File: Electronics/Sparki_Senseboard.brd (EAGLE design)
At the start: 88.7 x 17.1 mm, 21 parts

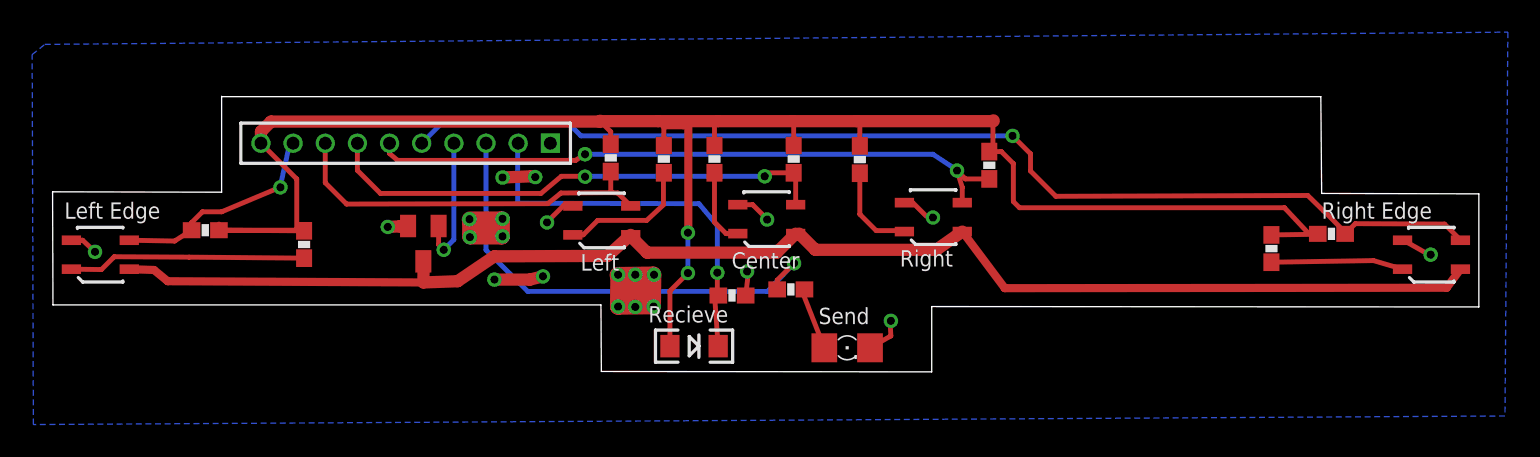
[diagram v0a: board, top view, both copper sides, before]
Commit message: Updated connectors, sensor multiplexing
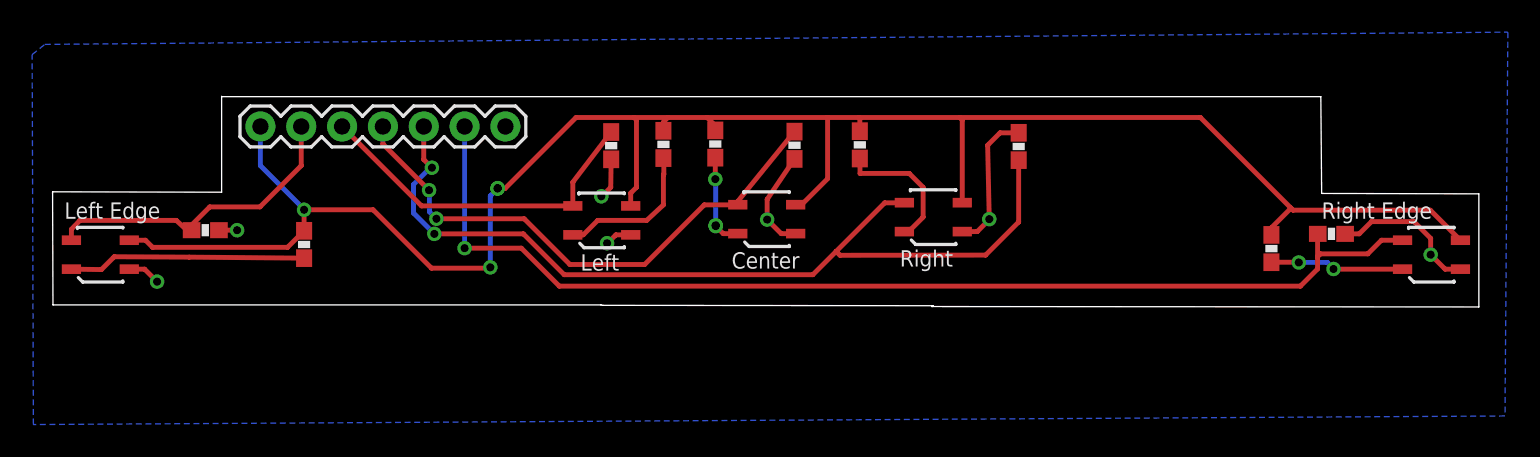
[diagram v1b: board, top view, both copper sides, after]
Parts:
- removed D4: IR_GRAB_LED, arcbotics:FKIT-LED-1206
- removed Q9: (no value), adafruit:SOT23
- removed R25: 100, SparkFun-Passives:0603-RES
- removed R26: 10k, SparkFun-Passives:0603-RES
- removed U$17: IR_GRAB_SENSE, arcbotics:LED-1206
- JP1: value M102MM -> (none); device arcbotics:1X10-2MM -> SparkFun-Connectors:1X07
- moved JP1 2.98 mm to (-16.3, 5.79)
- moved R16 2.17 mm to (15.6, 4.55), turned to 90 degrees
- moved R14 0.94 mm to (-3.23, 4.70)
- moved R15 0.91 mm to (-6.45, 4.67)
- moved R13 0.91 mm to (5.77, 4.65)
- moved R17 0.87 mm to (1.70, 4.62)
- moved R18 0.76 mm to (-9.70, 4.60)
- turned R21 to 0 degrees
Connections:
- removed net IR_GRAB_LED: JP1.3, R25.1
- removed net IR_GRAB_SENSE: JP1.2, R26.1, U$17.C
- removed net IR_SWITCH: JP1.4, Q9.1
- removed net N$25: Q9.3, U$10.2, U$4.2, U$5.2, U$6.2, U$9.2
- removed net N$33: D4.A, R25.2
- net GND: now also R16.2, R17.2, R18.2, R20.2, R21.2, U$10.2, U$4.2, U$5.2, U$6.2, U$9.2; no longer D4.C, Q9.2, R26.2, U$10.4, U$4.4, U$5.4, U$6.4, U$9.4
- net PB4: now also JP1.5, R18.1, U$6.4; no longer JP1.8, R18.2, U$6.3
- net PD4: now also JP1.3, R16.1, U$4.4; no longer JP1.6, R16.2, U$4.3
- net PD6: now also JP1.4, R17.1, U$5.4; no longer JP1.7, R17.2, U$5.3
- net PF5: now also JP1.6, R21.1, U$9.4; no longer JP1.9, R21.2, U$9.3
- net PF6: now also JP1.2, R20.1, U$10.4; no longer JP1.5, R20.2, U$10.3
- net VCC: now also JP1.7, U$10.3, U$4.3, U$5.3, U$6.3, U$9.3; no longer JP1.10, R16.1, R17.1, R18.1, R20.1, R21.1, U$17.A
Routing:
- net N$25: track 89.5 -> 0.00 mm
- net IR_GRAB_LED: track 29.6 -> 0.00 mm, vias 1 -> 0
- net IR_GRAB_SENSE: track 24.4 -> 0.00 mm, vias 1 -> 0
- net PD4: track 40.8 -> 56.3 mm
- net IR_SWITCH: track 8.50 -> 0.00 mm, vias 1 -> 0
- net GND: track 40.5 -> 32.0 mm, vias 22 -> 7
- net VCC: track 116.7 -> 124.7 mm, vias 2 -> 3
- net PF5: track 13.6 -> 19.7 mm, vias 1 -> 0
- net N$33: track 3.95 -> 0.00 mm
- net LINEFLEDLEFT: track 5.75 -> 8.60 mm
- net PD6: track 32.1 -> 34.4 mm
- net PB4: track 23.9 -> 21.8 mm
- net LINEFLEDMID: track 4.81 -> 5.83 mm, vias 0 -> 1
- net LINEFLEDRIGHT: track 8.30 -> 9.32 mm
- net N$1: track 8.23 -> 8.34 mm, vias 0 -> 1
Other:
- board size 88.7 x 17.1 mm -> 88.7 x 13.1 mm
- board text added: "RC2"
- board text removed: "RC1"
- board text removed: "Recieve"
- board text removed: "Rev1"
- board text removed: "Send"
